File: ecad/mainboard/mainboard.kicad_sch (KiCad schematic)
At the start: 57 parts, among them J1 TYPE-C-31-M-12, J2 SWD, J3 UART, SW1 TS-1187A-B-A-B, SW2 TS-1187A-B-A-B, SW3 SW_Push, SW4 SW_Push, U1 NCP1117ST33T3G, U2 USBLC6-2SC6, U2 W25Q128JVS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

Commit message: Made a top-plate for Udong Mainboard
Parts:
- added R6: 20k, Resistor_SMD:R_0402_1005Metric, symbol Device:R
- D2: value SK6812MINI -> SK6812MINI-E; JLCPCB (none) -> C5149201
- D3: JLCPCB (none) -> C5149201
- R4: value 40k -> 20k
- SW3, SW4: JLCPCB (none) -> C5156480
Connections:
- net REF_0.6V: now also R6.1; no longer R4.1
- new net: R4.1, R6.2
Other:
- moved on the sheet: R4
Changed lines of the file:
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@@
 	(wire
 		(pts
+			(xy 210.82 41.91) (xy 210.82 38.1)
+		)
+		(stroke
+			(width 0)
+			(type default)
+		)
+	)
+	(wire
+		(pts
 			(xy 191.77 137.16) (xy 195.58 137.16)
 		)
@@
 	(wire
 		(pts
-			(xy 210.82 41.91) (xy 210.82 38.1)
-		)
-		(stroke
-			(width 0)
-			(type default)
-		)
-	)
-	(wire
-		(pts
 			(xy 223.52 198.12) (xy 223.52 200.66)
 		)
@@
 	)
 	(symbol
+		(lib_id "Device:R")
+		(at 210.82 45.72 0)
+		(unit 1)
+		(exclude_from_sim no)
+		(in_bom yes)
+		(on_board yes)
+		(dnp no)
+		(fields_autoplaced yes)
+		(property "Reference" "R6"
+			(at 213.36 44.4499 0)
+			(effects
+				(font
+					(size 1.27 1.27)
+				)
+				(justify left)
+			)
+		)
+		(property "Value" "20k"
+			(at 213.36 46.9899 0)
+			(effects
+				(font
+					(size 1.27 1.27)
+				)
+				(justify left)
+			)
+		)
+		(property "Footprint" "Resistor_SMD:R_0402_1005Metric"
+			(at 209.042 45.72 90)
+			(effects
+				(font
+					(size 1.27 1.27)
+				)
+				(hide yes)
+			)
+		)
+		(property "Datasheet" "~"
+			(at 210.82 45.72 0)
+			(effects
+				(font
+					(size 1.27 1.27)
+				)
+				(hide yes)
+			)
+		)
+		(property "Description" "Resistor"
+			(at 210.82 45.72 0)
+			(effects
+				(font
+					(size 1.27 1.27)
+				)
+				(hide yes)
+			)
+		)
+		(pin "2"
+		)
+		(pin "1"
+		)
+		(instances
+			(project "mainboard"
+				(path "/b1313647-8d60-4294-add7-71c03651cfe3"
+					(reference "R6")
+					(unit 1)
+				)
+			)
+		)
+	)
+	(symbol
 		(lib_id "power:GND")
 		(at 223.52 205.74 90)
@@
 			)
 		)
-		(property "Value" "SK6812MINI"
+		(property "Value" "SK6812MINI-E"
 			(at 328.93 217.2014 0)
 			(effects
@@
 			)
 		)
+		(property "JLCPCB" " C5149201"
+			(at 316.23 220.98 0)
+			(effects
+				(font
+					(size 1.27 1.27)
+				)
+				(hide yes)
+			)
+		)
 		(pin "2"
 		)
@@
 			)
 		)
+		(property "JLCPCB" "C5156480"
+			(at 375.92 199.39 0)
+			(effects
+				(font
+					(size 1.27 1.27)
+				)
+				(hide yes)
+			)
+		)
 		(pin "1"
 		)
@@
 			)
 		)
+		(property "JLCPCB" "C5156480"
+			(at 321.31 200.66 0)
+			(effects
+				(font
+					(size 1.27 1.27)
+				)
+				(hide yes)
+			)
+		)
 		(pin "1"
 		)
@@
 			)
 		)
+		(property "JLCPCB" " C5149201"
+			(at 368.3 220.98 0)
+			(effects
+				(font
+					(size 1.27 1.27)
+				)
+				(hide yes)
+			)
+		)
 		(pin "2"
 		)
@@
 	(symbol
 		(lib_id "Device:R")
-		(at 210.82 45.72 0)
+		(at 210.82 53.34 0)
 		(unit 1)
 		(exclude_from_sim no)
@@
 		(fields_autoplaced yes)
 		(property "Reference" "R4"
-			(at 213.36 44.4499 0)
+			(at 213.36 52.0699 0)
 			(effects
 				(font
@@
 			)
 		)
-		(property "Value" "40k"
-			(at 213.36 46.9899 0)
+		(property "Value" "20k"
+			(at 213.36 54.6099 0)
 			(effects
 				(font
@@
 		)
 		(property "Footprint" "Resistor_SMD:R_0402_1005Metric"
-			(at 209.042 45.72 90)
+			(at 209.042 53.34 90)
 			(effects
 				(font
@@
 		)
 		(property "Datasheet" "~"
-			(at 210.82 45.72 0)
+			(at 210.82 53.34 0)
 			(effects
 				(font
@@
 		)
 		(property "Description" "Resistor"
-			(at 210.82 45.72 0)
+			(at 210.82 53.34 0)
 			(effects
 				(font
@@
 		(lib_name "GND_5")
 		(lib_id "power:GND")
-		(at 210.82 49.53 0)
+		(at 210.82 57.15 0)
 		(unit 1)
 		(exclude_from_sim no)
@@
 		(fields_autoplaced yes)
 		(property "Reference" "#PWR010"
-			(at 210.82 55.88 0)
+			(at 210.82 63.5 0)
 			(effects
 				(font
@@
 		)
 		(property "Value" "GND"
-			(at 210.82 54.61 0)
+			(at 210.82 62.23 0)
 			(effects
 				(font
@@
 		)
 		(property "Footprint" ""
-			(at 210.82 49.53 0)
+			(at 210.82 57.15 0)
 			(effects
 				(font
@@
 		)
 		(property "Datasheet" ""
-			(at 210.82 49.53 0)
+			(at 210.82 57.15 0)
 			(effects
 				(font
@@
 		)
 		(property "Description" "Power symbol creates a global label with name \"GND\" , ground"
-			(at 210.82 49.53 0)
+			(at 210.82 57.15 0)
 			(effects
 				(font

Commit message: WIP: PCB case
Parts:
- C10, C8: value 1u -> 1uF
- D1: JCSC (none) -> C2297; JLCPCB C2297 -> (none)
- D2: value SK6812MINI-E -> SK6812MINI-EA; JCSC (none) -> C5378731; JLCPCB C5149201 -> (none)
- D3: value SK6812MINI -> SK6812MINI-EA; JCSC (none) -> C5378731; JLCPCB C5149201 -> (none)
- J1: footprint Connector_USB:USB_C_Receptacle_HRO_TYPE-C-31-M-12 -> Udong:USB_C_Receptacle_HRO_TYPE-C-31-M-12; JCSC (none) -> C165948; JLCPCB C165948 -> (none)
- J2: footprint Connector_JST:JST_SH_BM03B-SRSS-TB_1x03-1MP_P1.00mm_Vertical -> Udong:JST_SH_BM03B-SRSS-TB_1x03-1MP_P1.00mm_Vertical; JCSC (none) -> C160403; JLCPCB C160403 -> (none)
- SW1, SW2: JCSC (none) -> C318884; JLCPCB C318884 -> (none)
- U1: JCSC (none) -> C26537; JLCPCB C26537 -> (none)
- U2: JCSC (none) -> C2827654; JLCPCB C2827654 -> (none)
- U4: JCSC (none) -> C2676173; JLCPCB C2676173 -> (none)
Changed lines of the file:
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@@
 			)
 		)
-		(property "Value" "1u"
+		(property "Value" "1uF"
 			(at 156.591 138.303 0)
 			(effects
@@
 			)
 		)
-		(property "Value" "1u"
+		(property "Value" "1uF"
 			(at 211.201 138.303 0)
 			(effects
@@
 			)
 		)
-		(property "JLCPCB" "C318884"
+		(property "JCSC" "C318884"
 			(at 350.52 67.31 0)
 			(effects
@@
 			)
 		)
-		(property "Footprint" "Connector_JST:JST_SH_BM03B-SRSS-TB_1x03-1MP_P1.00mm_Vertical"
+		(property "Footprint" "Udong:JST_SH_BM03B-SRSS-TB_1x03-1MP_P1.00mm_Vertical"
 			(at 349.25 97.79 0)
 			(effects
@@
 			)
 		)
-		(property "JLCPCB" "C160403"
+		(property "JCSC" "C160403"
 			(at 349.25 97.79 0)
 			(effects
@@
 		(fields_autoplaced yes)
 		(property "Reference" "D2"
-			(at 328.93 214.6614 0)
+			(at 330.2 214.6614 0)
 			(effects
 				(font
@@
 			)
 		)
-		(property "Value" "SK6812MINI-E"
-			(at 328.93 217.2014 0)
+		(property "Value" "SK6812MINI-EA"
+			(at 330.2 217.2014 0)
 			(effects
 				(font
@@
 			)
 		)
-		(property "JLCPCB" " C5149201"
+		(property "JCSC" "C5378731"
 			(at 316.23 220.98 0)
 			(effects
@@
 			)
 		)
-		(property "JLCPCB" "C2827654"
+		(property "JCSC" "C2827654"
 			(at 81.28 49.53 0)
 			(effects
@@
 			)
 		)
-		(property "JLCPCB" "C2297"
+		(property "JCSC" "C2297"
 			(at 353.06 127 0)
 			(effects
@@
 		(fields_autoplaced yes)
 		(property "Reference" "D3"
-			(at 381 214.6614 0)
+			(at 382.27 214.6614 0)
 			(effects
 				(font
@@
 			)
 		)
-		(property "Value" "SK6812MINI"
-			(at 381 217.2014 0)
+		(property "Value" "SK6812MINI-EA"
+			(at 382.27 217.2014 0)
 			(effects
 				(font
@@
 			)
 		)
-		(property "JLCPCB" " C5149201"
+		(property "JCSC" "C5378731"
 			(at 368.3 220.98 0)
 			(effects
@@
 			)
 		)
-		(property "Footprint" "Connector_USB:USB_C_Receptacle_HRO_TYPE-C-31-M-12"
+		(property "Footprint" "Udong:USB_C_Receptacle_HRO_TYPE-C-31-M-12"
 			(at 38.1 49.53 0)
 			(effects
@@
 			)
 		)
-		(property "JLCPCB" "C165948"
+		(property "JCSC" "C165948"
 			(at 34.29 49.53 0)
 			(effects
@@
 			)
 		)
-		(property "JLCPCB" "C318884"
+		(property "JCSC" "C318884"
 			(at 350.52 55.88 0)
 			(effects
@@
 			)
 		)
-		(property "JLCPCB" "C2676173"
+		(property "JCSC" "C2676173"
 			(at 302.26 184.15 0)
 			(effects
@@
 			)
 		)
-		(property "JLCPCB" "C26537"
+		(property "JCSC" "C26537"
 			(at 168.91 36.83 0)
 			(effects

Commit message: prepare for the rev.1 board
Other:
- note added: "TODO: DO_NOT_USE REF_0.6 it's connected to Digital Input...."
- note added: "TODO: Stop using GPID23, 24. It might be better NOT to use GPIOs which has special purpose on Rasberry Pi Pico. It may enable us to keep using the Rasberry Pi board for development. GPIO23 Controls the on-board SMPS power save pin. GPIO24 Senses voltage at VBUS pin - high if VBUS is present, else low. GPIO25 Connected to onboard LED. GPIO29 Used in ADC mode (ADC3) to measure VSYS/3."
- moved on the sheet: C16, C17, D2, D3, R12, SW3, SW4, U4

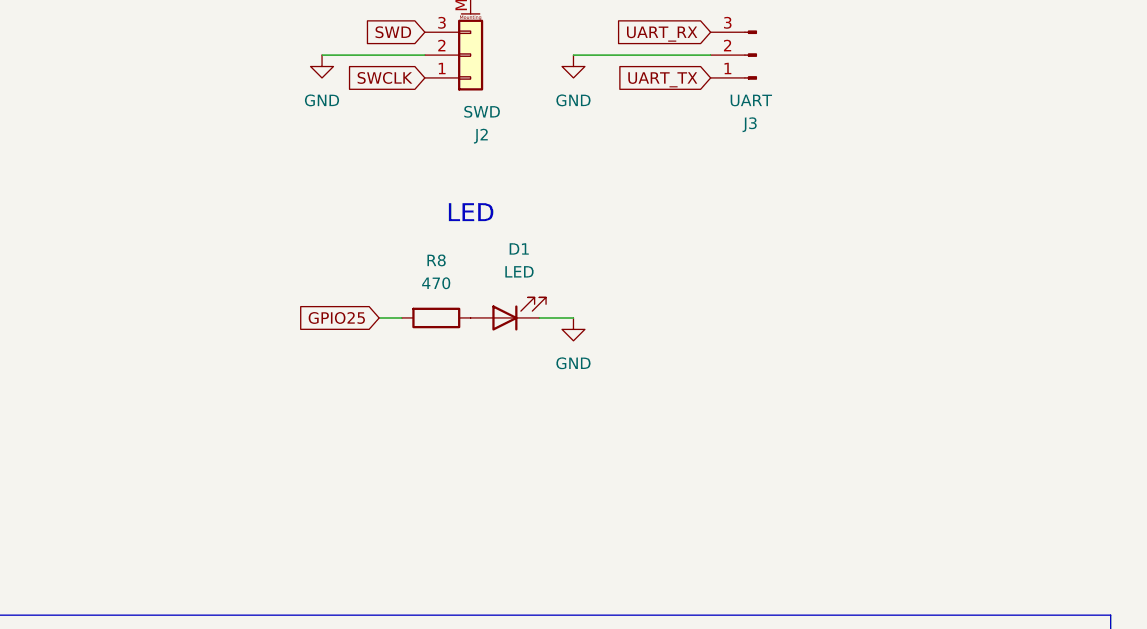
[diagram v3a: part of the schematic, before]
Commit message: Configure platformio to use Debug Probe
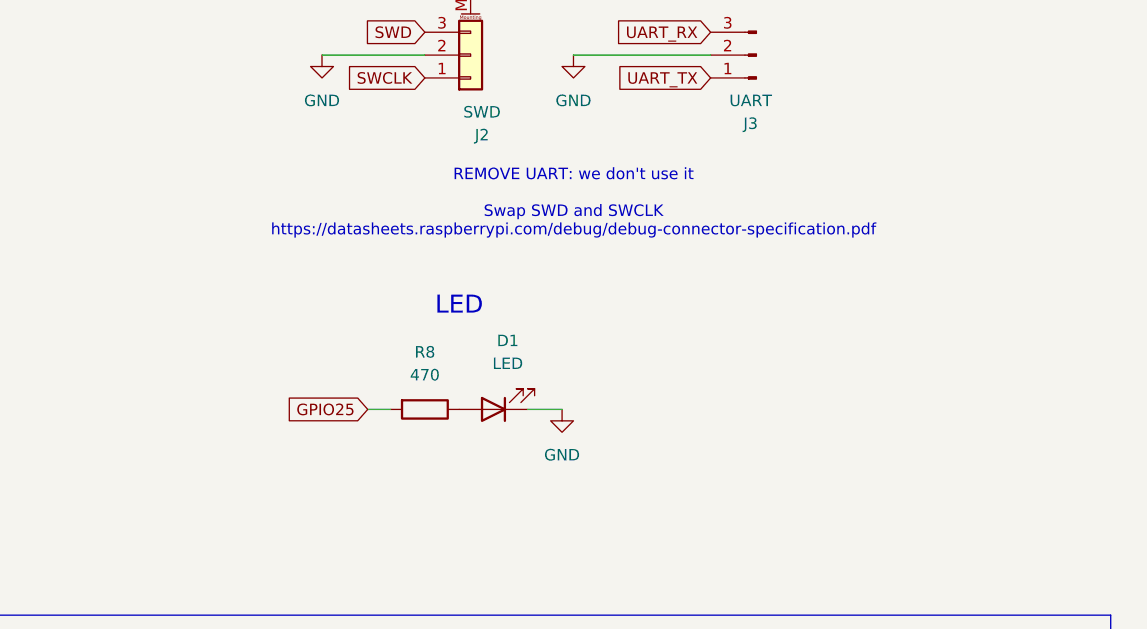
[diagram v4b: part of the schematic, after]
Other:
- note added: "REMOVE UART: we don't use it Swap SWD and SWCLK https://datasheets.raspberrypi.com/debug/debug-connector-specification.pdf"
- moved on the sheet: D1, R8
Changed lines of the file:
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@@
 	(wire
 		(pts
-			(xy 356.87 127) (xy 360.68 127)
+			(xy 355.6 137.16) (xy 359.41 137.16)
 		)
 		(stroke
@@
 	(wire
 		(pts
-			(xy 339.09 127) (xy 341.63 127)
+			(xy 337.82 137.16) (xy 340.36 137.16)
 		)
 		(stroke
@@
 	(text "LED"
 		(exclude_from_sim no)
-		(at 349.25 115.57 0)
+		(at 347.98 125.73 0)
 		(effects
 			(font
@@
 		)
 	)
+	(text "REMOVE UART: we don't use it\n\nSwap SWD and SWCLK\nhttps://datasheets.raspberrypi.com/debug/debug-connector-specification.pdf"
+		(exclude_from_sim no)
+		(at 360.68 114.3 0)
+		(effects
+			(font
+				(size 1.27 1.27)
+			)
+		)
+	)
 	(text "Differentional pair\n"
 		(exclude_from_sim no)
@@
 	(global_label "GPIO25"
 		(shape input)
-		(at 339.09 127 180)
+		(at 337.82 137.16 180)
 		(fields_autoplaced yes)
 		(effects
@@
 		)
 		(property "Intersheetrefs" "${INTERSHEET_REFS}"
-			(at 329.2105 127 0)
+			(at 327.9405 137.16 0)
 			(effects
 				(font
@@
 		(lib_name "GND_2")
 		(lib_id "power:GND")
-		(at 360.68 127 0)
+		(at 359.41 137.16 0)
 		(unit 1)
 		(exclude_from_sim no)
@@
 		(fields_autoplaced yes)
 		(property "Reference" "#PWR020"
-			(at 360.68 133.35 0)
+			(at 359.41 143.51 0)
 			(effects
 				(font
@@
 		)
 		(property "Value" "GND"
-			(at 360.68 132.08 0)
+			(at 359.41 142.24 0)
 			(effects
 				(font
@@
 		)
 		(property "Footprint" ""
-			(at 360.68 127 0)
+			(at 359.41 137.16 0)
 			(effects
 				(font
@@
 		)
 		(property "Datasheet" ""
-			(at 360.68 127 0)
+			(at 359.41 137.16 0)
 			(effects
 				(font
@@
 		)
 		(property "Description" "Power symbol creates a global label with name \"GND\" , ground"
-			(at 360.68 127 0)
+			(at 359.41 137.16 0)
 			(effects
 				(font
@@
 	(symbol
 		(lib_id "Device:LED")
-		(at 353.06 127 180)
+		(at 351.79 137.16 180)
 		(unit 1)
 		(exclude_from_sim no)
@@
 		(fields_autoplaced yes)
 		(property "Reference" "D1"
-			(at 354.6475 119.38 0)
+			(at 353.3775 129.54 0)
 			(effects
 				(font
@@
 		)
 		(property "Value" "LED"
-			(at 354.6475 121.92 0)
+			(at 353.3775 132.08 0)
 			(effects
 				(font
@@
 		)
 		(property "Footprint" "LED_SMD:LED_0805_2012Metric"
-			(at 353.06 127 0)
+			(at 351.79 137.16 0)
 			(effects
 				(font
@@
 		)
 		(property "Datasheet" "~"
-			(at 353.06 127 0)
+			(at 351.79 137.16 0)
 			(effects
 				(font
@@
 		)
 		(property "Description" "Light emitting diode"
-			(at 353.06 127 0)
+			(at 351.79 137.16 0)
 			(effects
 				(font
@@
 		)
 		(property "JCSC" "C2297"
-			(at 353.06 127 0)
+			(at 351.79 137.16 0)
 			(effects
 				(font
@@
 	(symbol
 		(lib_id "Device:R")
-		(at 345.44 127 270)
+		(at 344.17 137.16 270)
 		(unit 1)
 		(exclude_from_sim no)
@@
 		(fields_autoplaced yes)
 		(property "Reference" "R8"
-			(at 345.44 120.65 90)
+			(at 344.17 130.81 90)
 			(effects
 				(font
@@
 		)
 		(property "Value" "470"
-			(at 345.44 123.19 90)
+			(at 344.17 133.35 90)
 			(effects
 				(font
@@
 		)
 		(property "Footprint" "Resistor_SMD:R_0402_1005Metric"
-			(at 345.44 125.222 90)
+			(at 344.17 135.382 90)
 			(effects
 				(font
@@
 		)
 		(property "Datasheet" "~"
-			(at 345.44 127 0)
+			(at 344.17 137.16 0)
 			(effects
 				(font
@@
 		)
 		(property "Description" "Resistor"
-			(at 345.44 127 0)
+			(at 344.17 137.16 0)
 			(effects
 				(font

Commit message: Update circuit for the new design
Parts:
- removed C16, C17: 1uF, Capacitor_SMD:C_0402_1005Metric, symbol Device:C
- removed D2, D3: SK6812MINI-EA, Udong:MX_Socket_LED, symbol udong_library:SK6812MINI_1_FIXED
- removed J3: UART, Connector_PinSocket_2.54mm:PinSocket_1x03_P2.54mm_Horizontal, symbol Connector:Conn_01x03_Pin
- removed R12: 560, Resistor_SMD:R_0402_1005Metric, symbol Device:R
- removed R4, R6: 20k, Resistor_SMD:R_0402_1005Metric, symbol Device:R
- removed SW1, SW2: TS-1187A-B-A-B, Button_Switch_SMD:SW_Push_1P1T_XKB_TS-1187A, symbol Switch:SW_Push
- removed U4: 74AHCT1G125, Package_TO_SOT_SMD:SOT-353_SC-70-5, symbol 74xGxx:74AHCT1G125
- added R30, R9: 10k, Resistor_SMD:R_0402_1005Metric, symbol Device:R
- added R32: 1k, Resistor_SMD:R_0402_1005Metric, symbol Device:R
- R1: value 220k -> 10k
- R3, R4: footprint Resistor_SMD:R_0402_1005Metric -> Resistor_SMD:R_0603_1608Metric
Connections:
- net LED_OUT is gone; now on net GND: U3.36 (GPIO24)
- net REF_0.6V is gone; now on net GND: R1.2, U3.6 (GPIO4)
- net UART_RX is gone; now on net GND: U3.3 (GPIO1)
- net UART_TX is gone; now on net GND: U3.2 (GPIO0)
- net +3.3V: now also R30.1, R9.1; no longer R1.1
- net DS_0_IN: now also U3.4 (GPIO2); no longer U3.34 (GPIO22)
- net DS_1_IN: now also R5.2, U3.5 (GPIO3), R32.1; no longer SW4.1, U3.35 (GPIO23)
- net GND: now also U3.34 (GPIO22); no longer U3.4 (GPIO2), U3.5 (GPIO3)
- net QSPI_SS: now also R9.2
- net RUN: no longer names the net of U3.26 (RUN)
- new net: R1.1, U3.35 (GPIO23)
- new net BOOTSEL_SW: R30.2, R32.2, SW4.1
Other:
- note added: "1k is small enough compared to 10k pull-up"
- note added: "Digital switches"
- note added: "Don't use GPID23, 24, 25 and 29 It might be better NOT to use GPIOs which has special purpose on Rasberry Pi Pico. It may enable us to keep using the Rasberry Pi board for development. GPIO23 Controls the on-board SMPS power save pin. GPIO24 Senses voltage at VBUS pin - high if VBUS is present, else low. GPIO25 Connected to onboard LED. GPIO29 Used in ADC mode (ADC3) to measure VSYS/3."
- note added: "Make sure that BOOTSEL_SW is pulled-up even before RP2040 configuires IO settings."
- note added: "Prevent short circuit when GPIO23 is used as output (someone would try to control switching mode power supply)"
- note added: "Pull-up resistor for Flash"
- note added: "REMOVE UART: we don't use it triple check SWD and SWCLK https://datasheets.raspberrypi.com/debug/debug-connector-specification.pdf (confirmed that we used a bad footprint...) Put 100 Ohm resitors very close to the IC We further specify 'source termination' resistors on both pins at both ends of the link: - 100 Ohm resistor on the SC/TX and SD/RX IC pins at the host - 100 Ohm resistors on the SC/R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"
- note removed: "DNF"
- note removed: "Digital switches / LEDs"
- note removed: "Keep the output controll pin GND"
- note removed: "REMOVE UART: we don't use it Swap SWD and SWCLK https://datasheets.raspberrypi.com/debug/debug-connector-specification.pdf"
- note removed: "Reset/Bootsel switches"
- note removed: "TODO: DO_NOT_USE REF_0.6 it's connected to Digital Input...."
- note removed: "TODO: Stop using GPID23, 24. It might be better NOT to use GPIOs which has special purpose on Rasberry Pi Pico. It may enable us to keep using the Rasberry Pi board for development. GPIO23 Controls the on-board SMPS power save pin. GPIO24 Senses voltage at VBUS pin - high if VBUS is present, else low. GPIO25 Connected to onboard LED. GPIO29 Used in ADC mode (ADC3) to measure VSYS/3."
- note removed: "This flash strage doesn't require a pull-up registor here (@R9) However, some other device would require a pull-up registor so let me put a DNF registor for the record."
- moved on the sheet: C5, D1, J2, R8, SW3, SW4, U2

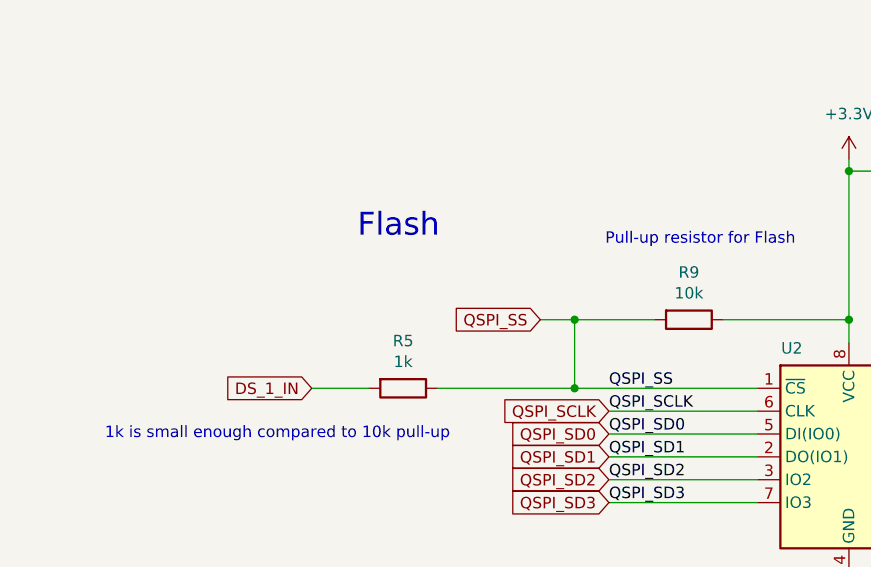
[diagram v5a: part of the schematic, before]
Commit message: Update PCB. Next task would be move switch positions
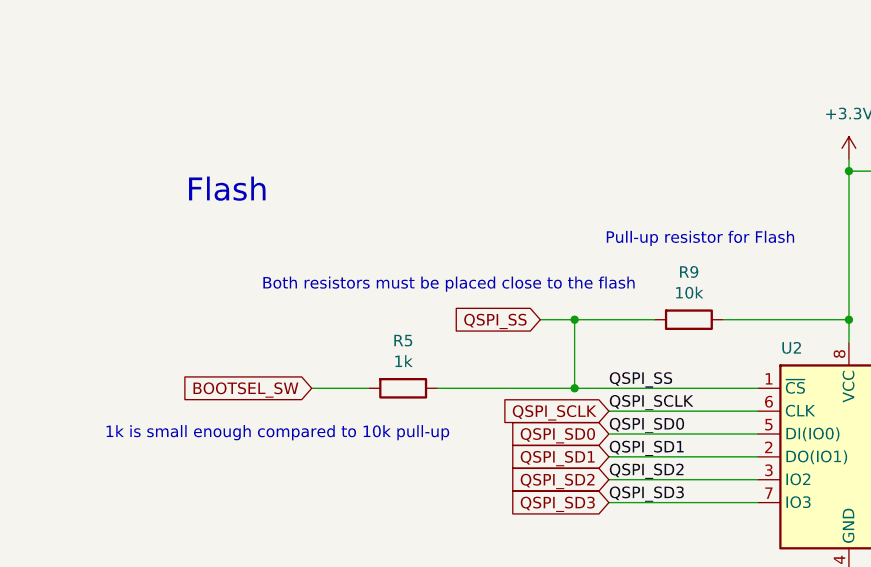
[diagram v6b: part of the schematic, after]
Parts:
- J2: footprint Udong:JST_SH_BM03B-SRSS-TB_1x03-1MP_P1.00mm_Vertical -> Connector_JST:JST_SH_SM03B-SRSS-TB_1x03-1MP_P1.00mm_Horizontal
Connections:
- net BOOTSEL_SW: now also R5.2
- net DS_1_IN: no longer R5.2
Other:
- note added: "Both resistors must be placed close to the flash"
